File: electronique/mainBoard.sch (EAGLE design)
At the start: 32 parts, among them IC1 L298, IC2 7805TV

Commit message: MAJ electronique (final version)
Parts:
- added JP2: (no value), pinhead:PINHD-1X3
- added LED_LOW_BATT, LED_POWER, LED_STARTING...: (no value), led:LED3MM
- added R4: (no value), resistor:R-EU_0204/7
- added R5: (no value), resistor:R-EU_0207/2V
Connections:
- net N$6 renamed MOTOR_EXT
- new net LOW_BATT: LED_LOW_BATT.A, U$1.29
- new net N$7: LED_POWER.C, R4.2
- new net N$9: LED_LOW_BATT.C, LED_STARTING....C, R5.2
- new net STARTING...: LED_STARTING....A, U$1.30
- new net START_SIGNAL: JP2.1, U$1.A11
- net +3V3: now also JP2.2, LED_POWER.A
- net GND: now also JP2.3, R4.1, R5.1
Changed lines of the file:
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@@
 <part name="JP1" library="pinhead" deviceset="PINHD-1X2" device=""/>
 <part name="SUPPLY35" library="supply2" deviceset="+7V" device=""/>
+<part name="JP2" library="pinhead" deviceset="PINHD-1X3" device=""/>
+<part name="+3V15" library="supply1" deviceset="+3V3" device=""/>
+<part name="SUPPLY36" library="supply2" deviceset="GND" device=""/>
+<part name="LED_POWER" library="led" deviceset="LED" device="3MM"/>
+<part name="LED_LOW_BATT" library="led" deviceset="LED" device="3MM"/>
+<part name="LED_STARTING..." library="led" deviceset="LED" device="3MM"/>
+<part name="R4" library="resistor" deviceset="R-EU_" device="0204/7"/>
+<part name="R5" library="resistor" deviceset="R-EU_" device="0207/2V"/>
+<part name="SUPPLY37" library="supply2" deviceset="GND" device=""/>
+<part name="SUPPLY38" library="supply2" deviceset="GND" device=""/>
+<part name="+3V16" library="supply1" deviceset="+3V3" device=""/>
 </parts>
 <sheets>
@@
 <instance part="JP1" gate="G$1" x="68.58" y="-15.24" rot="R90"/>
 <instance part="SUPPLY35" gate="G$1" x="76.2" y="-17.78"/>
+<instance part="JP2" gate="A" x="104.14" y="-15.24" rot="R90"/>
+<instance part="+3V15" gate="G$1" x="104.14" y="-33.02" rot="R180"/>
+<instance part="SUPPLY36" gate="GND" x="106.68" y="-22.86"/>
+<instance part="LED_POWER" gate="G$1" x="132.08" y="-17.78"/>
+<instance part="LED_LOW_BATT" gate="G$1" x="144.78" y="-17.78"/>
+<instance part="LED_STARTING..." gate="G$1" x="160.02" y="-17.78"/>
+<instance part="R4" gate="G$1" x="132.08" y="-33.02" rot="R90"/>
+<instance part="R5" gate="G$1" x="152.4" y="-33.02" rot="R90"/>
+<instance part="SUPPLY37" gate="GND" x="132.08" y="-40.64"/>
+<instance part="SUPPLY38" gate="GND" x="152.4" y="-40.64"/>
+<instance part="+3V16" gate="G$1" x="132.08" y="-2.54"/>
 </instances>
 <busses>
@@
 <pinref part="SUPPLY34" gate="GND" pin="GND"/>
 </segment>
+<segment>
+<pinref part="JP2" gate="A" pin="3"/>
+<wire x1="106.68" y1="-17.78" x2="106.68" y2="-20.32" width="0.1524" layer="91"/>
+<pinref part="SUPPLY36" gate="GND" pin="GND"/>
+</segment>
+<segment>
+<pinref part="R4" gate="G$1" pin="1"/>
+<pinref part="SUPPLY37" gate="GND" pin="GND"/>
+</segment>
+<segment>
+<pinref part="R5" gate="G$1" pin="1"/>
+<pinref part="SUPPLY38" gate="GND" pin="GND"/>
+</segment>
 </net>
 <net name="+5V" class="0">
@@
 <pinref part="+3V14" gate="G$1" pin="+3V3"/>
 <wire x1="-30.48" y1="-25.4" x2="-35.56" y2="-25.4" width="0.1524" layer="91"/>
+</segment>
+<segment>
+<pinref part="JP2" gate="A" pin="2"/>
+<wire x1="104.14" y1="-17.78" x2="104.14" y2="-30.48" width="0.1524" layer="91"/>
+<pinref part="+3V15" gate="G$1" pin="+3V3"/>
+</segment>
+<segment>
+<pinref part="LED_POWER" gate="G$1" pin="A"/>
+<pinref part="+3V16" gate="G$1" pin="+3V3"/>
+<wire x1="132.08" y1="-5.08" x2="132.08" y2="-15.24" width="0.1524" layer="91"/>
 </segment>
 </net>
@@
 </segment>
 </net>
-<net name="N$6" class="0">
+<net name="START_SIGNAL" class="0">
+<segment>
+<pinref part="JP2" gate="A" pin="1"/>
+<wire x1="101.6" y1="-17.78" x2="101.6" y2="-25.4" width="0.1524" layer="91"/>
+<label x="101.6" y="-25.4" size="1.778" layer="95" rot="R180" xref="yes"/>
+</segment>
+<segment>
+<pinref part="U$1" gate="G$1" pin="A11"/>
+<wire x1="53.34" y1="25.4" x2="55.88" y2="25.4" width="0.1524" layer="91"/>
+<label x="55.88" y="25.4" size="1.778" layer="95" xref="yes"/>
+</segment>
+</net>
+<net name="N$7" class="0">
+<segment>
+<pinref part="LED_POWER" gate="G$1" pin="C"/>
+<pinref part="R4" gate="G$1" pin="2"/>
+<wire x1="132.08" y1="-27.94" x2="132.08" y2="-22.86" width="0.1524" layer="91"/>
+</segment>
+</net>
+<net name="N$9" class="0">
+<segment>
+<pinref part="LED_LOW_BATT" gate="G$1" pin="C"/>
+<wire x1="144.78" y1="-22.86" x2="144.78" y2="-25.4" width="0.1524" layer="91"/>
+<wire x1="144.78" y1="-25.4" x2="152.4" y2="-25.4" width="0.1524" layer="91"/>
+<pinref part="R5" gate="G$1" pin="2"/>
+<wire x1="152.4" y1="-25.4" x2="152.4" y2="-27.94" width="0.1524" layer="91"/>
+<pinref part="LED_STARTING..." gate="G$1" pin="C"/>
+<wire x1="160.02" y1="-22.86" x2="160.02" y2="-25.4" width="0.1524" layer="91"/>
+<wire x1="160.02" y1="-25.4" x2="152.4" y2="-25.4" width="0.1524" layer="91"/>
+<junction x="152.4" y="-25.4"/>
+</segment>
+</net>
+<net name="LOW_BATT" class="0">
+<segment>
+<pinref part="U$1" gate="G$1" pin="29"/>
+<wire x1="22.86" y1="10.16" x2="17.78" y2="10.16" width="0.1524" layer="91"/>
+<label x="17.78" y="10.16" size="1.778" layer="95" rot="R180" xref="yes"/>
+</segment>
+<segment>
+<pinref part="LED_LOW_BATT" gate="G$1" pin="A"/>
+<wire x1="144.78" y1="-15.24" x2="144.78" y2="-10.16" width="0.1524" layer="91"/>
+<label x="144.78" y="-10.16" size="1.778" layer="95" rot="R90" xref="yes"/>
+</segment>
+</net>
+<net name="STARTING..." class="0">
+<segment>
+<pinref part="U$1" gate="G$1" pin="30"/>
+<wire x1="22.86" y1="7.62" x2="17.78" y2="7.62" width="0.1524" layer="91"/>
+<label x="17.78" y="7.62" size="1.778" layer="95" rot="R180" xref="yes"/>
+</segment>
+<segment>
+<pinref part="LED_STARTING..." gate="G$1" pin="A"/>
+<wire x1="160.02" y1="-15.24" x2="160.02" y2="-10.16" width="0.1524" layer="91"/>
+<label x="160.02" y="-10.16" size="1.778" layer="95" rot="R90" xref="yes"/>
+</segment>
+</net>
+<net name="MOTOR_EXT" class="0">
 <segment>
 <pinref part="U$1" gate="G$1" pin="28"/>
 <wire x1="22.86" y1="12.7" x2="17.78" y2="12.7" width="0.1524" layer="91"/>
-<wire x1="17.78" y1="12.7" x2="17.78" y2="-27.94" width="0.1524" layer="91"/>
+<label x="17.78" y="12.7" size="1.778" layer="95" rot="R180" xref="yes"/>
+</segment>
+<segment>
 <pinref part="R3" gate="G$1" pin="1"/>
-<wire x1="17.78" y1="-27.94" x2="50.8" y2="-27.94" width="0.1524" layer="91"/>
-</segment>
-</net>
+<wire x1="45.72" y1="-27.94" x2="50.8" y2="-27.94" width="0.1524" layer="91"/>
+<label x="45.72" y="-27.94" size="1.778" layer="95" rot="R180" xref="yes"/>
+</segment>
+</net>

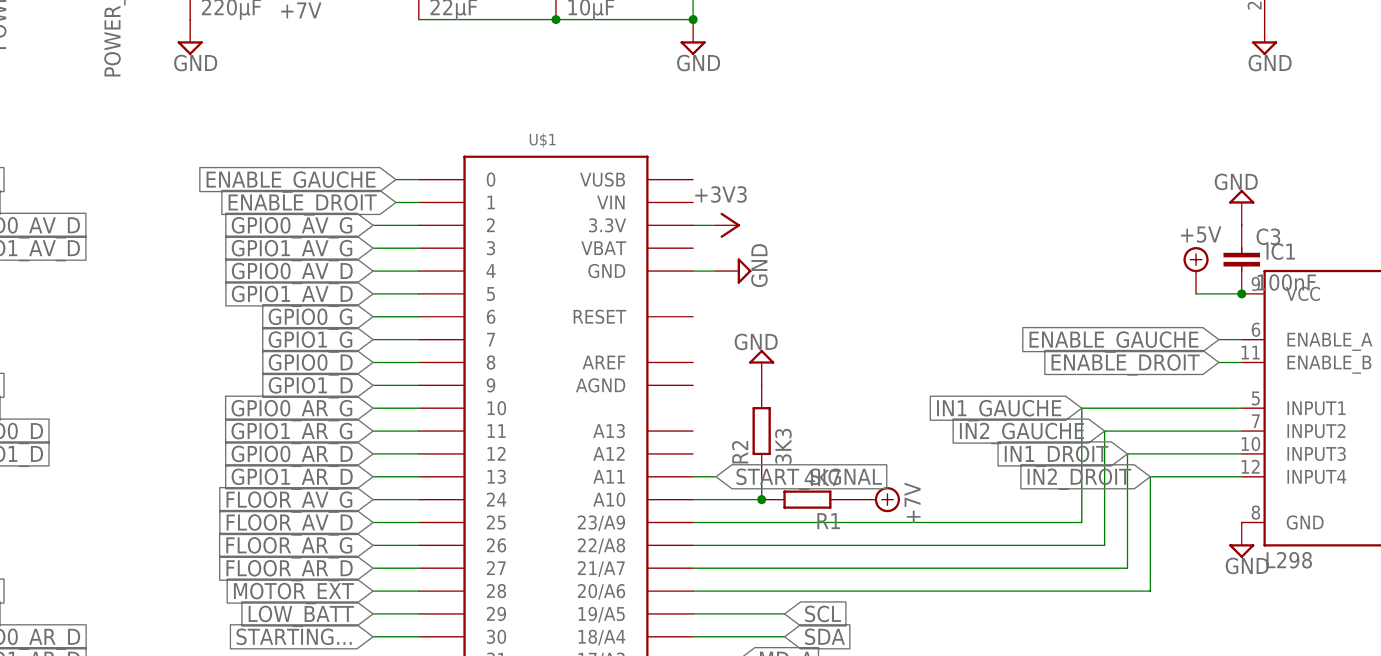
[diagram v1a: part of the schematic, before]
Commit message: control des moteurs OK + controle tension des lipos fonctionnel
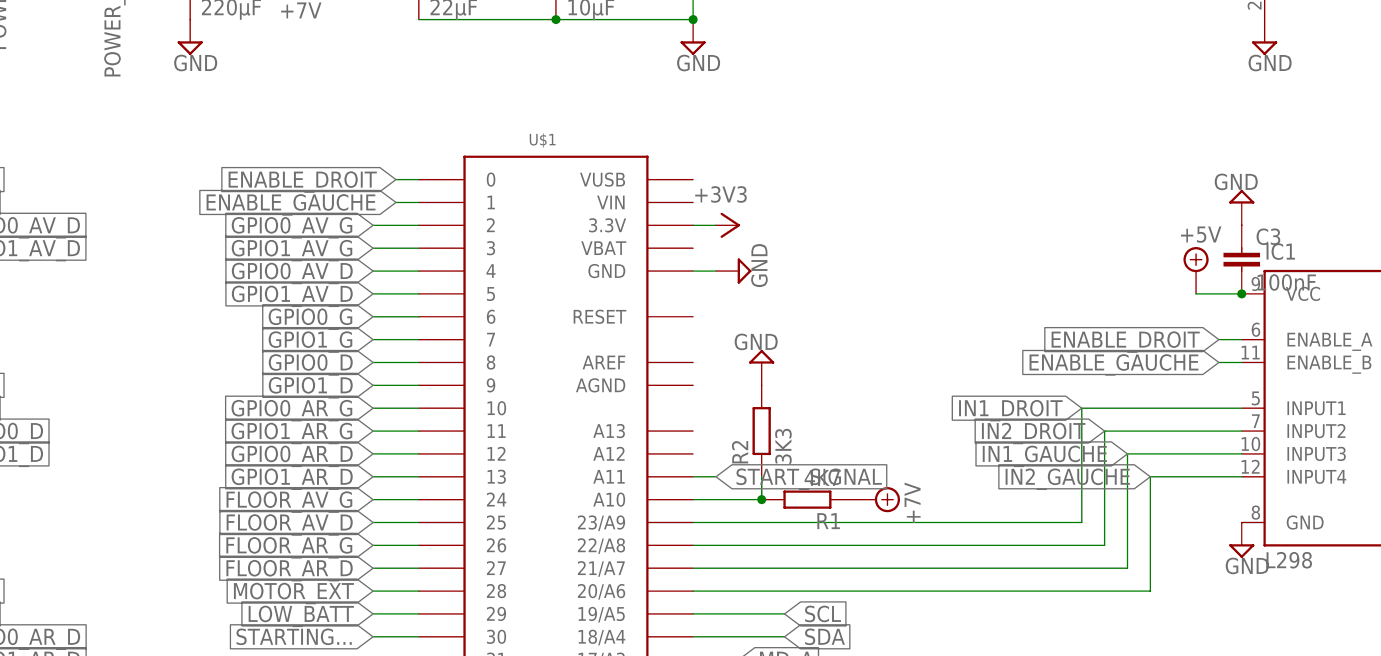
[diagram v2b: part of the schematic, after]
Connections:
- net ENABLE_DROIT: now also IC1.ENABLE_A, U$1.0; no longer IC1.ENABLE_B, U$1.1
- net ENABLE_GAUCHE: now also IC1.ENABLE_B, U$1.1; no longer IC1.ENABLE_A, U$1.0
- net IN1_DROIT: now also IC1.INPUT1, U$1.23/A9; no longer IC1.INPUT3, U$1.21/A7
- net IN1_GAUCHE: now also IC1.INPUT3, U$1.21/A7; no longer IC1.INPUT1, U$1.23/A9
- net IN2_DROIT: now also IC1.INPUT2, U$1.22/A8; no longer IC1.INPUT4, U$1.20/A6
- net IN2_GAUCHE: now also IC1.INPUT4, U$1.20/A6; no longer IC1.INPUT2, U$1.22/A8
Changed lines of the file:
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@@
 </segment>
 </net>
-<net name="ENABLE_GAUCHE" class="0">
+<net name="ENABLE_DROIT" class="0">
 <segment>
 <pinref part="IC1" gate="L298" pin="ENABLE_A"/>
@@
 </segment>
 </net>
-<net name="ENABLE_DROIT" class="0">
+<net name="ENABLE_GAUCHE" class="0">
 <segment>
 <pinref part="IC1" gate="L298" pin="ENABLE_B"/>
@@
 </segment>
 </net>
-<net name="IN1_GAUCHE" class="0">
+<net name="IN1_DROIT" class="0">
 <segment>
 <pinref part="IC1" gate="L298" pin="INPUT1"/>
@@
 </segment>
 </net>
-<net name="IN2_GAUCHE" class="0">
+<net name="IN2_DROIT" class="0">
 <segment>
 <pinref part="IC1" gate="L298" pin="INPUT2"/>
@@
 </segment>
 </net>
-<net name="IN1_DROIT" class="0">
+<net name="IN1_GAUCHE" class="0">
 <segment>
 <pinref part="IC1" gate="L298" pin="INPUT3"/>
@@
 </segment>
 </net>
-<net name="IN2_DROIT" class="0">
+<net name="IN2_GAUCHE" class="0">
 <segment>
 <pinref part="IC1" gate="L298" pin="INPUT4"/>
